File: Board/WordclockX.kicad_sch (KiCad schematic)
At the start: 103 parts, among them J1 USB_C_Receptacle_USB2.0, SW1 SW_Push, U1 RP2040, U2 PCA9626, U3 PCA9626, U4 MCP7940N-xST, U5 MIC5504-3.3YM5, U6 W25Q16JLSNIG, U7 74HCT137, Y1 12M, Y2 32768

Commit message: Some additions to the schematic
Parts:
- removed SW1: SW_Push, symbol Switch:SW_Push
- removed SW2: ~, symbol Switch:SW_Push
- added D1, D2, D3, D4: blue, LED_SMD:LED_0603_1608Metric, symbol Device:LED
- added R12, R13, R14, R15: 680, Resistor_SMD:R_0603_1608Metric, symbol Device:R
- added SW1, SW2: SW_Push_Dual, Button_Switch_SMD:SW_Push_1P1T_NO_CK_KSC6xxJ, symbol Switch:SW_Push_Dual
- renumbered C10 to C1, C2 to C10, C3 to C11, C1 to C12, C4 to C13, C9 to C2, C8 to C3, C12 to C4, C11 to C5, C7 to C6, C5 to C7, C6 to C8, C13 to C9, D1 to D5, D2 to D6, R58 to R1, R55 to R10, R56 to R11, R25 to R16, R32 to R17, R10 to R18, R12 to R19, R57 to R2, R14 to R20, R16 to R21, R28 to R22, R33 to R23, R37 to R24, R41 to R25, R9 to R26, R11 to R27, R13 to R28, R15 to R29, R61 to R3, R26 to R30, R30 to R31, R35 to R32, R39 to R33, R24 to R34, R47 to R35, R23 to R36, R43 to R37, R22 to R38, R48 to R39, R60 to R4, R21 to R40, R44 to R41, R20 to R42, R49 to R43, R19 to R44, R18 to R46, R50 to R47, R17 to R48, R46 to R49, R59 to R5, R1 to R50, R3 to R51, R5 to R52, R7 to R53, R27 to R54, R31 to R55, R36 to R56, R40 to R57, R2 to R58, R4 to R59, R51 to R6, R6 to R60, R8 to R61, R29 to R62, R34 to R63, R38 to R64, R42 to R65, R52 to R7, R53 to R8, R54 to R9, TP5 to TP1, TP6 to TP2, TP1 to TP3, TP2 to TP4, TP3 to TP5, TP4 to TP6, U6 to U1, U4 to U2, U1 to U3, U5 to U4, U7 to U5, U2 to U6, U3 to U7
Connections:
- net GND: now also D5.S, D6.S, D1.1 (K), D2.1 (K), D3.1 (K), D4.1 (K), SW1.3, SW2.3
- net at R5.2, U3.26 (RUN): now also SW1.2
- net at R1.2: now also SW2.2
- new net: D2.2 (A), R13.1
- new net: D3.2 (A), R14.1
- new net: D1.2 (A), R12.1
- new net: D4.2 (A), R15.1
- new net LED1: R12.2
- new net LED2: R13.2
- new net LED3: R14.2
- new net LED4: R15.2
- no-connect marks 2 -> 6
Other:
- note added: "- GPIO Zuordnung - Kondensator an LED-Versorgung und MCU - DCF77 vorsehen: Antennenhalter, Kondensator + Verstärker - USB-Protection"
- note removed: "- GPIO Zuordnung - Kondensator an LED-Versorgung - Steckverbinder für LED-Matrix - DCF77 vorsehen (Antennenhalter, Kondensator + Verstärker) - Reset-, Boot-Taster - Status LED - USB-Protection"
- moved on the sheet: BT1, C1, C2, C3, C4, C5, C6, C7, C8, J1, R1, R10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

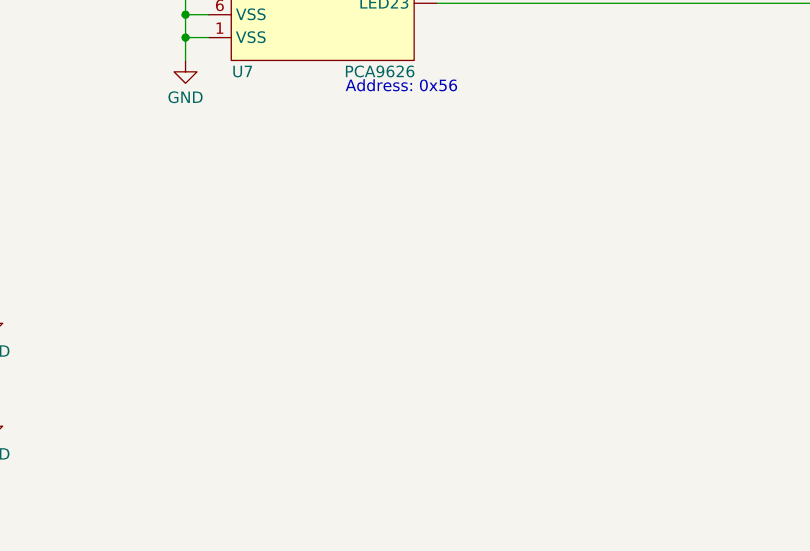
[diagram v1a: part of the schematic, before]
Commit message: Sized our board and placed LEDs to final location
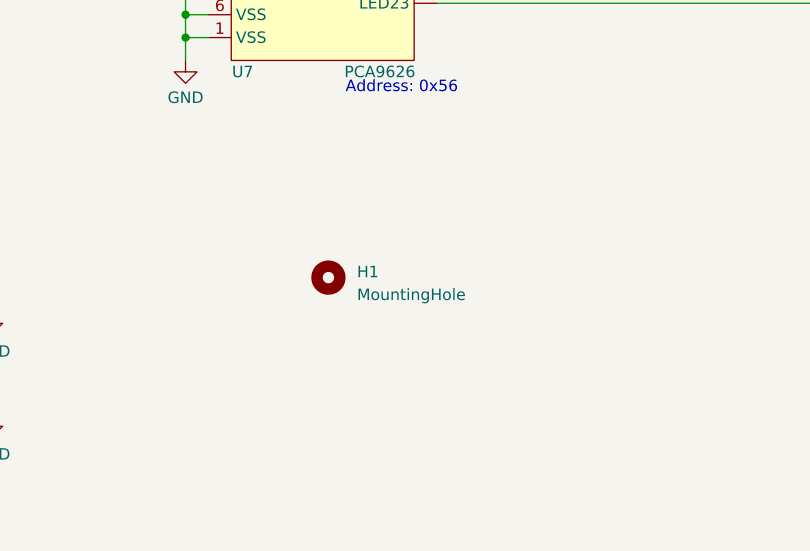
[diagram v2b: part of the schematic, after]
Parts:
- added H1: MountingHole, symbol Mechanical:MountingHole
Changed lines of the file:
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@@
+    )
+  )
+  (symbol (lib_id "Mechanical:MountingHole") (at 307.975 247.65 0) (unit 1)
+    (in_bom yes) (on_board yes) (dnp no) (fields_autoplaced)
+    (property "Reference" "H1" (at 311.15 247.015 0)
+      (effects (font (size 1.27 1.27)) (justify left))
+    )
+    (property "Value" "MountingHole" (at 311.15 249.555 0)
+      (effects (font (size 1.27 1.27)) (justify left))
+    )
+    (property "Footprint" "" (at 307.975 247.65 0)
+      (effects (font (size 1.27 1.27)) hide)
+    )
+    (property "Datasheet" "~" (at 307.975 247.65 0)
+      (effects (font (size 1.27 1.27)) hide)
+    )
+    (property "Mouser" "534-24882" (at 307.975 247.65 0)
+      (effects (font (size 1.27 1.27)) hide)
+    )
+    (instances
+      (project "WordclockX"
+        (path "/8cd55a18-23dc-4682-bd3c-80c7cacd7e8a"
+          (reference "H1") (unit 1)
+        )
+      )
     )
   )

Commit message: Added capacitors and pin assignments, also new footprint for LED array without holes
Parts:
- added C11: 10u, symbol Device:C
- added C16, C19: 1u, symbol Device:C
- added C17, C18, C20, C21, C22, C23, C24, C25, C26: 100n, symbol Device:C
- added C9: 500u, 25V, symbol Device:C_Polarized
- added D1, D2: ~, Package_DFN_QFN:Diodes_UDFN-10_1.0x2.5mm_P0.5mm, symbol Wordclock:SP1064E-04UTG
- added R12: 10k, Resistor_SMD:R_0603_1608Metric, symbol Device:R
- D7: renamed from D5; footprint Wordclock:2088RGB-5 -> Wordclock:2088RGB-5_no-holes
- D8: renamed from D6; footprint Wordclock:2088RGB-5 -> Wordclock:2088RGB-5_no-holes
- R2: renamed from R5; value 1k -> 10k
- R3: renamed from R2; value DNP -> 10k; now not fitted
- renumbered C9 to C10, C10 to C12, C11 to C13, C12 to C14, C13 to C15, D1 to D3, D2 to D4, D3 to D5, D4 to D6, R12 to R13, R13 to R14, R14 to R15, R15 to R16, R16 to R17, R17 to R18, R18 to R19, R19 to R20, R20 to R21, R21 to R22, R22 to R23, R23 to R24, R24 to R25, R25 to R26, R26 to R27, R27 to R28, R28 to R29, R29 to R30, R30 to R31, R31 to R32, R32 to R33, R33 to R34, R34 to R35, R35 to R36, R36 to R37, R37 to R38, R38 to R39, R3 to R4, R39 to R40, R40 to R41, R41 to R42, R42 to R43, R43 to R44, R44 to R45, R45 to R46, R46 to R47, R47 to R48, R48 to R49, R4 to R5, R49 to R50, R50 to R51, R51 to R52, R52 to R53, R53 to R54, R54 to R55, R55 to R56, R56 to R57, R57 to R58, R58 to R59, R59 to R60, R60 to R61, R61 to R62, R62 to R63, R63 to R64, R64 to R65, R65 to R66
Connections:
- net +5V: now also C11.1, C9.1
- net GND: now also C11.2, C16.2, C17.2, C18.2, C19.2, C20.2, C21.2, C22.2, C23.2, C24.2, C25.2, C26.2, C9.2, D1.3 (GND), D1.8 (GND), D2.3 (GND), D2.8 (GND), R12.2
- net I2C_SCL: now also U3.3 (GPIO1)
- net I2C_SDA: now also U3.2 (GPIO0)
- net LED1: now also U3.13 (GPIO10)
- net LED2: now also U3.14 (GPIO11)
- net LED3: now also U3.15 (GPIO12)
- net LED4: now also U3.16 (GPIO13)
- net ROWSEL_A0: now also U3.6 (GPIO4)
- net ROWSEL_A1: now also U3.7 (GPIO5)
- net ROWSEL_A2: now also U3.8 (GPIO6)
- net ROWSEL_EN: now also U3.11 (GPIO8), R12.1
- net ROWSEL_LE: now also U3.9 (GPIO7)
- net RTC_MFP: now also U3.12 (GPIO9)
- net TOUCH0: now also U3.38 (GPIO26_ADC0), D2.2 (Ch.2)
- net TOUCH1: now also U3.39 (GPIO27_ADC1), D2.1 (Ch.1)
- net TOUCH2: now also U3.40 (GPIO28_ADC2), D2.4 (Ch.3)
- net TOUCH3: now also U3.41 (GPIO29_ADC3), D2.5 (Ch.4)
- net USB_DM: now also D1.1 (Ch.1)
- net USB_DP: now also D1.2 (Ch.2)
- net VCC: now also U3.1 (IOVDD), U3.10 (IOVDD), U3.22 (IOVDD), U3.33 (IOVDD), U3.42 (IOVDD), U3.43 (ADC_AVDD), U3.44 (VREG_IN), U3.48 (USB_VDD), U3.49 (IOVDD), C19.1, C20.1, C21.1, C22.1, C23.1, C24.1, C25.1, C26.1
- net DRIVER2_OE: now reaches R18.2, U7.24 (OE)
- net DRIVER2_OE: now also U3.5 (GPIO3)
- net DRIVER1_OE: now reaches R17.2, U6.24 (OE)
- net DRIVER1_OE: now also U3.4 (GPIO2)
- net +1V1: now reaches U3.23 (DVDD), U3.50 (DVDD)
- net +1V1: now also U3.45 (VREG_VOUT), C16.1, C17.1, C18.1
- no-connect marks 6 -> 8
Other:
- note added: "- Kondensatoren für LED-Versorgung heraussuchen - DCF77 vorsehen: Antennenhalter, Kondensator + Verstärker"
- note added: "1u - Pin 45 100n - Pins 23, 50"
- note added: "1u - Pins 44 / 45 100n - Pins 1, 10, 22, 33, 42, 48, 49"
- note removed: "- GPIO Zuordnung - Kondensator an LED-Versorgung und MCU - DCF77 vorsehen: Antennenhalter, Kondensator + Verstärker - USB-Protection"
- moved on the sheet: C12, C13, D3, D4, D5, D6, R10, R11, R2, R6, R7, R8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

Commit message: Placed some resistors
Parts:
- U2: footprint (none) -> Package_SO:TSSOP-8_4.4x3mm_P0.65mm
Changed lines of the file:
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@@
       (effects (font (size 1.27 1.27)) (justify left))
     )
-    (property "Footprint" "" (at 80.01 96.52 0)
+    (property "Footprint" "Package_SO:TSSOP-8_4.4x3mm_P0.65mm" (at 80.01 96.52 0)
       (effects (font (size 1.27 1.27)) hide)
     )

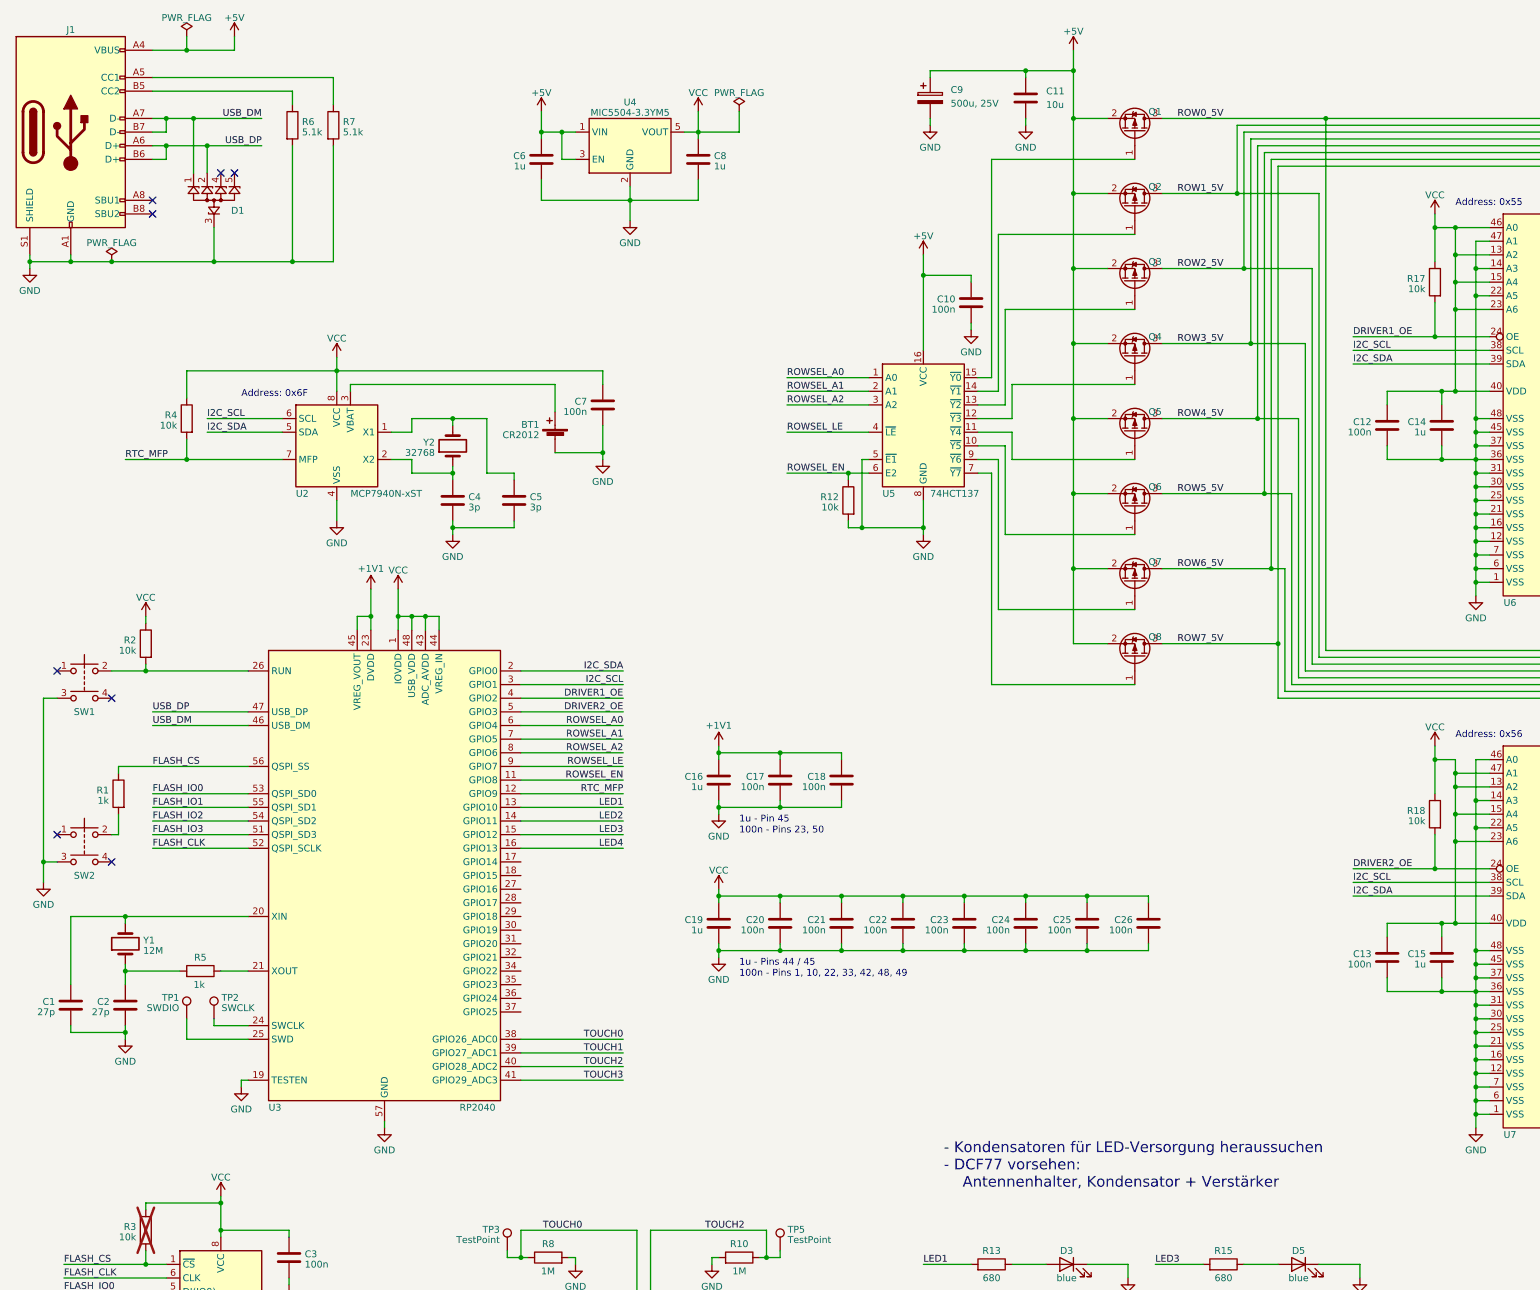
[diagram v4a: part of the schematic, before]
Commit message: Started adding DC/DC converter for LED supply
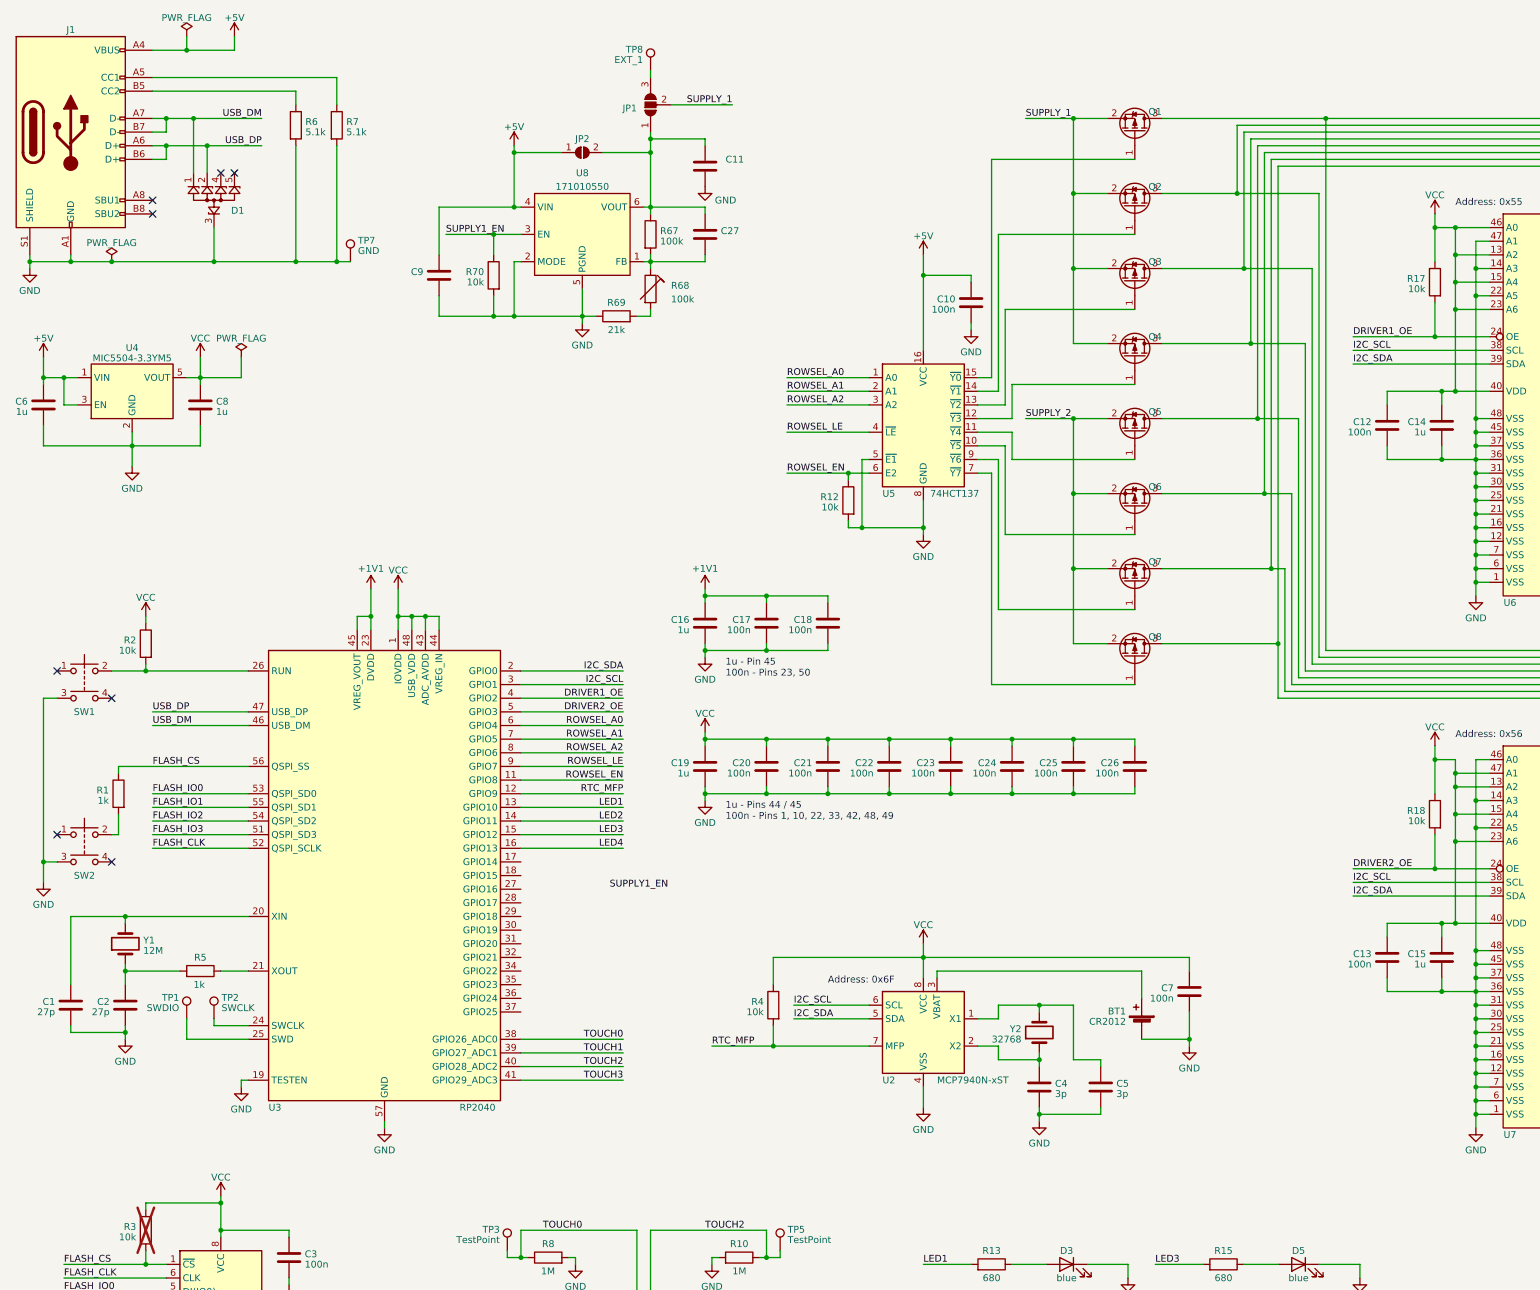
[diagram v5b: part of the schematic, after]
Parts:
- removed C9: 500u, 25V, symbol Device:C_Polarized
- added C27, C9: ~, symbol Device:C
- added JP1: SolderJumper_3_Open, symbol Jumper:SolderJumper_3_Open
- added JP2: SolderJumper_2_Open, symbol Jumper:SolderJumper_2_Open
- added R67: 100k, Resistor_SMD:R_0603_1608Metric, symbol Device:R
- added R68: 100k, symbol Device:R_Trim
- added R69: 21k, Resistor_SMD:R_0603_1608Metric, symbol Device:R
- added R70: 10k, Resistor_SMD:R_0603_1608Metric, symbol Device:R
- added TP7: GND, symbol Connector:TestPoint
- added TP8: EXT_1, symbol Connector:TestPoint
- added U8: 171010550, Wordclock:LGA-6EP_2.5x2.5, symbol Wordclock:171010550
- C11: value 10u -> ~
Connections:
- net +5V: now also C9.1, JP2.1 (A), U8.4 (VIN); no longer C11.1, Q1.2 (S), Q2.2 (S), Q3.2 (S), Q4.2 (S), Q5.2 (S), Q6.2 (S), Q7.2 (S), Q8.2 (S)
- net GND: now also C9.2, R69.1, R70.2, TP7.1, U8.2 (MODE), U8.5 (PGND), U8.EP (PGND)
- net ROW0_5V: no longer names the net of D7.17 (C1), D8.17 (C1), Q1.3 (D)
- net ROW1_5V: no longer names the net of D7.18 (C2), D8.18 (C2), Q2.3 (D)
- net ROW2_5V: no longer names the net of D7.19 (C3), D8.19 (C3), Q3.3 (D)
- net ROW3_5V: no longer names the net of D7.20 (C4), D8.20 (C4), Q4.3 (D)
- net ROW4_5V: no longer names the net of D7.29 (C5), D8.29 (C5), Q5.3 (D)
- net ROW5_5V: no longer names the net of D7.30 (C6), D8.30 (C6), Q6.3 (D)
- net ROW6_5V: no longer names the net of D7.31 (C7), D8.31 (C7), Q7.3 (D)
- net ROW7_5V: no longer names the net of D7.32 (C8), D8.32 (C8), Q8.3 (D)
- new net: C27.2, R67.2, R68.1, U8.1 (FB)
- new net: R68.2, R69.2
- new net: C11.1, C27.1, JP1.1 (A), JP2.2 (B), R67.1, U8.6 (VOUT)
- new net: JP1.3 (B), TP8.1
- new net SUPPLY1_EN: R70.1, U8.3 (EN)
- new net SUPPLY_1: JP1.2 (C), Q1.2 (S), Q2.2 (S), Q3.2 (S), Q4.2 (S)
- new net SUPPLY_2: Q5.2 (S), Q6.2 (S), Q7.2 (S), Q8.2 (S)
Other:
- note removed: "- Kondensatoren für LED-Versorgung heraussuchen - DCF77 vorsehen: Antennenhalter, Kondensator + Verstärker"
- moved on the sheet: BT1, C11, C16, C17, C18, C19, C20, C21, C22, C23, C24, C25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
